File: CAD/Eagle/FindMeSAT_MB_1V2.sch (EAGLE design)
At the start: 135 parts, among them Q101 ABS07-32.768KHZ, Q651 ABM3B-16MHZ-10-R50-1-U, U1001 CFPT-141-20MHZ, U101 ATXMEGA256A3BU-AU, U1011 OPA354, U1021 OPA354, U1111 LM2831YMF, U1121 LM4120IM5-3.0, U201 SIM808, U301 MPU-9250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

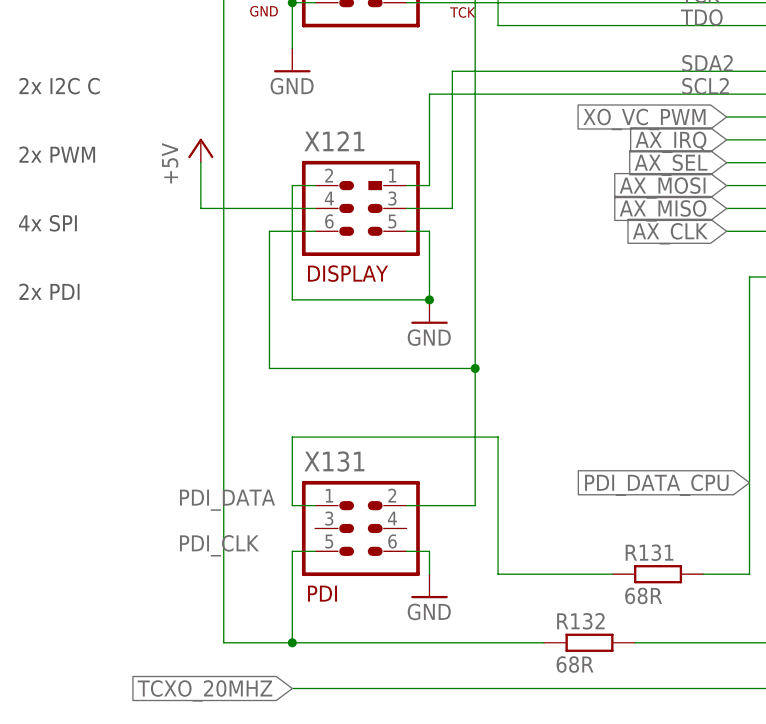
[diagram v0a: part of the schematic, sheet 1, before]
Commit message: HW_V1.2 - LCD connector swapped
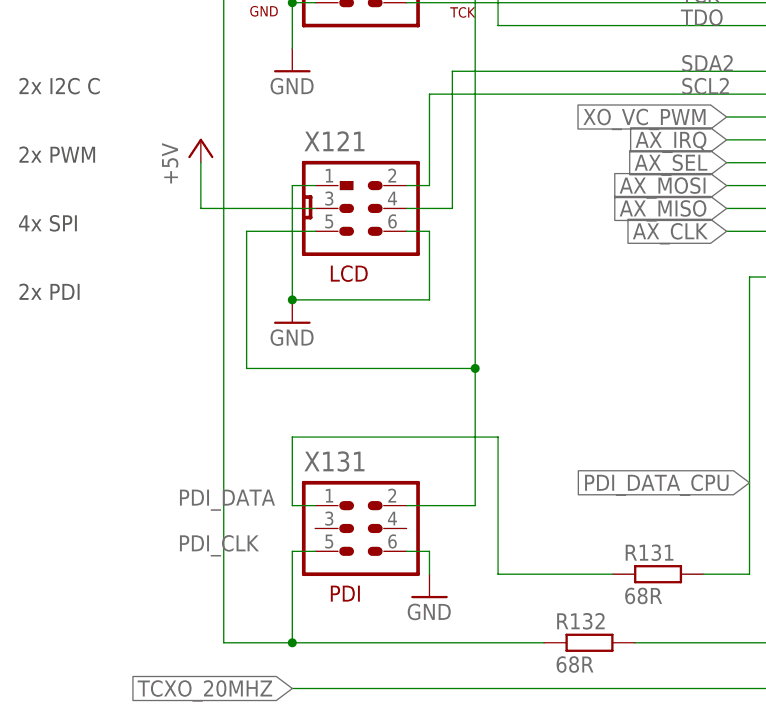
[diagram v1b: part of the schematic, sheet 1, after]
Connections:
- net +3V3: now also X121.5; no longer X121.6
- net +5V: now also X121.3; no longer X121.4
- net GND: now also X121.1, X121.6; no longer X121.2, X121.5
- net SCL2: now also X121.2; no longer X121.1
- net SDA2: now also X121.4; no longer X121.3
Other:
- note added: "LCD"
- note removed: "DISPLAY"
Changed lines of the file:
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@@
 <plain>
 <text x="132.08" y="66.04" size="1.778" layer="97">XTAL 1</text>
-<text x="37.084" y="35.052" size="1.778" layer="94" ratio="10">PDI</text>
+<text x="39.624" y="35.052" size="1.778" layer="94" ratio="10">PDI</text>
 <text x="5.08" y="114.3" size="1.778" layer="97">2x ADC B Audio</text>
 <text x="5.08" y="129.54" size="1.778" layer="97">8x ADC A MEAS</text>
@@
 <text x="5.08" y="68.58" size="1.778" layer="97">2x PDI</text>
 <text x="5.08" y="109.22" size="1.778" layer="97">2x DAC B Audio</text>
-<text x="37.084" y="70.612" size="1.778" layer="94" ratio="10">DISPLAY</text>
+<text x="39.624" y="70.612" size="1.778" layer="94" ratio="10">LCD</text>
 <text x="94.234" y="157.226" size="1.778" layer="94" ratio="10">I/O</text>
 </plain>
@@
 <attribute name="NAME" x="36.83" y="85.09" size="2.1844" layer="95" ratio="10"/>
 </instance>
-<instance part="GND121" gate="1" x="50.8" y="66.04"/>
+<instance part="GND121" gate="1" x="35.56" y="66.04"/>
 <instance part="+5V1" gate="G$1" x="25.4" y="86.36"/>
 <instance part="X181" gate="G$1" x="100.33" y="165.1" smashed="yes">
@@
 <segment>
 <pinref part="GND121" gate="1" pin="GND"/>
-<wire x1="50.8" y1="68.58" x2="50.8" y2="76.2" width="0.1524" layer="91"/>
-<pinref part="X121" gate="G$1" pin="5"/>
-<wire x1="50.8" y1="76.2" x2="48.26" y2="76.2" width="0.1524" layer="91"/>
+<wire x1="35.56" y1="68.58" x2="35.56" y2="81.28" width="0.1524" layer="91"/>
+<pinref part="X121" gate="G$1" pin="1"/>
+<wire x1="35.56" y1="81.28" x2="38.1" y2="81.28" width="0.1524" layer="91"/>
+<pinref part="X121" gate="G$1" pin="6"/>
+<wire x1="48.26" y1="76.2" x2="50.8" y2="76.2" width="0.1524" layer="91"/>
+<wire x1="50.8" y1="76.2" x2="50.8" y2="68.58" width="0.1524" layer="91"/>
 <wire x1="50.8" y1="68.58" x2="35.56" y2="68.58" width="0.1524" layer="91"/>
-<wire x1="35.56" y1="68.58" x2="35.56" y2="81.28" width="0.1524" layer="91"/>
-<pinref part="X121" gate="G$1" pin="2"/>
-<wire x1="35.56" y1="81.28" x2="38.1" y2="81.28" width="0.1524" layer="91"/>
-<junction x="50.8" y="68.58"/>
+<junction x="35.56" y="68.58"/>
 </segment>
 <segment>
@@
 <pinref part="X111" gate="G$1" pin="7"/>
 <pinref part="+3V3_121" gate="G$1" pin="+3V3"/>
-<wire x1="55.88" y1="60.96" x2="33.02" y2="60.96" width="0.1524" layer="91"/>
-<wire x1="33.02" y1="60.96" x2="33.02" y2="76.2" width="0.1524" layer="91"/>
-<pinref part="X121" gate="G$1" pin="6"/>
-<wire x1="33.02" y1="76.2" x2="38.1" y2="76.2" width="0.1524" layer="91"/>
+<wire x1="55.88" y1="60.96" x2="30.48" y2="60.96" width="0.1524" layer="91"/>
+<wire x1="30.48" y1="60.96" x2="30.48" y2="76.2" width="0.1524" layer="91"/>
+<pinref part="X121" gate="G$1" pin="5"/>
+<wire x1="30.48" y1="76.2" x2="38.1" y2="76.2" width="0.1524" layer="91"/>
 <junction x="55.88" y="60.96"/>
 </segment>
@@
 <label x="78.74" y="93.98" size="1.778" layer="95"/>
 <wire x1="53.34" y1="93.98" x2="53.34" y2="78.74" width="0.1524" layer="91"/>
-<pinref part="X121" gate="G$1" pin="3"/>
+<pinref part="X121" gate="G$1" pin="4"/>
 <wire x1="53.34" y1="78.74" x2="48.26" y2="78.74" width="0.1524" layer="91"/>
 </segment>
@@
 <label x="78.74" y="91.44" size="1.778" layer="95"/>
 <wire x1="50.8" y1="91.44" x2="50.8" y2="81.28" width="0.1524" layer="91"/>
-<pinref part="X121" gate="G$1" pin="1"/>
+<pinref part="X121" gate="G$1" pin="2"/>
 <wire x1="50.8" y1="81.28" x2="48.26" y2="81.28" width="0.1524" layer="91"/>
 </segment>
@@
 <pinref part="+5V1" gate="G$1" pin="+5V"/>
 <wire x1="25.4" y1="83.82" x2="25.4" y2="78.74" width="0.1524" layer="91"/>
-<pinref part="X121" gate="G$1" pin="4"/>
+<pinref part="X121" gate="G$1" pin="3"/>
 <wire x1="25.4" y1="78.74" x2="38.1" y2="78.74" width="0.1524" layer="91"/>
 </segment>
